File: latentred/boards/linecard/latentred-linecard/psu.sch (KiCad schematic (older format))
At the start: 56 parts, among them U1 MCP1703T-3302E, U2 LTC3374-QFN, U3 SI7050, U4 LTC2451, U5 INA226, U6 INA226, U7 INA226

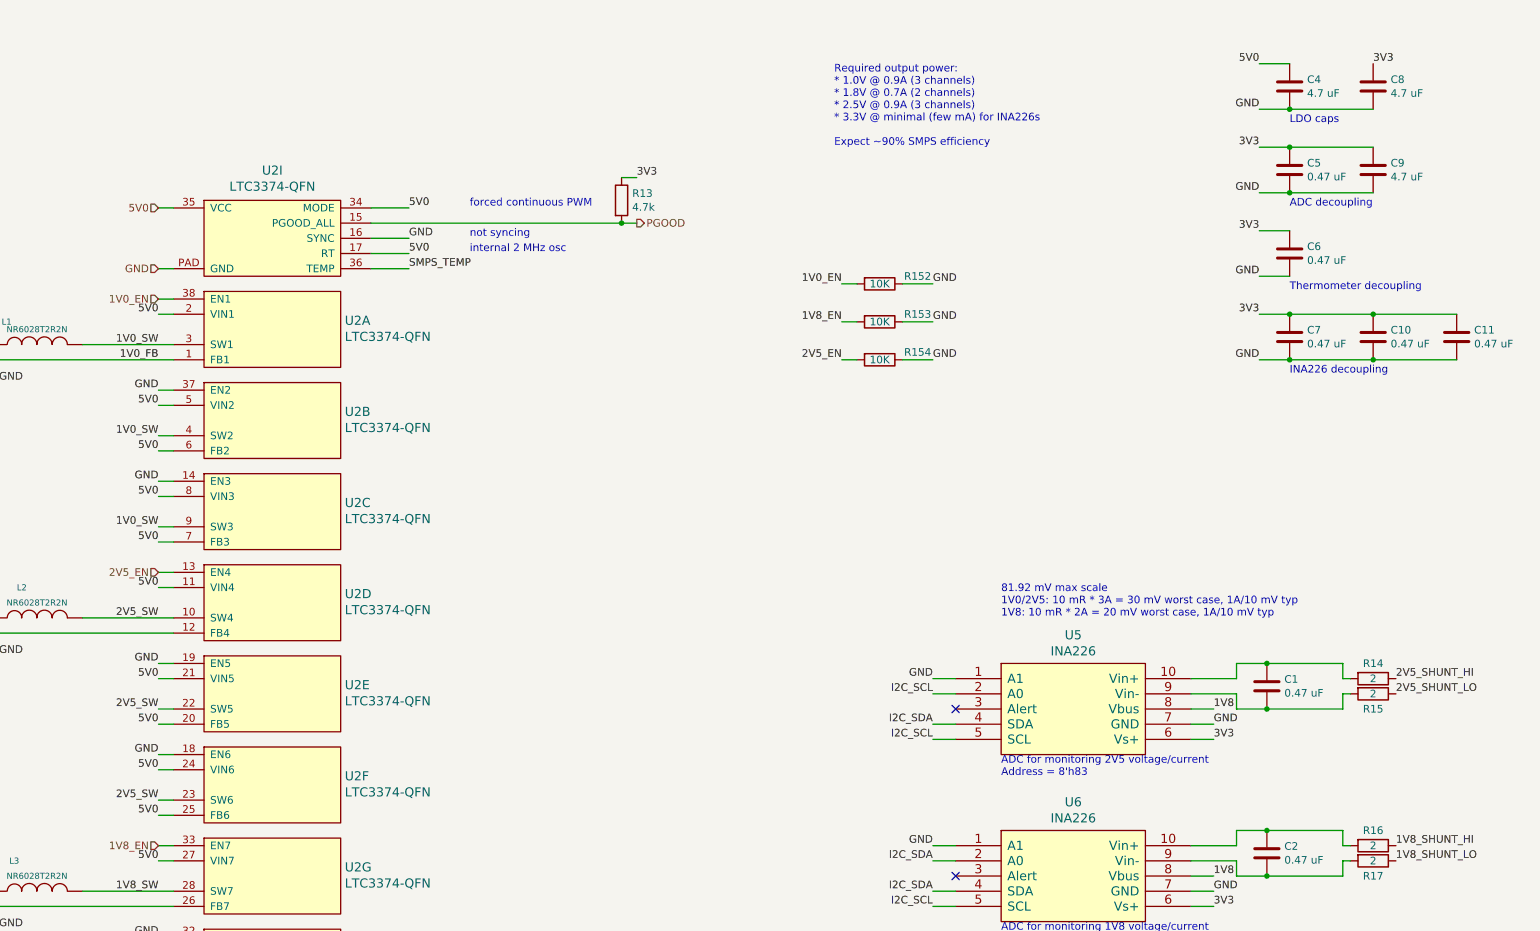
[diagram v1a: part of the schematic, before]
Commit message: Continued initial line card layout
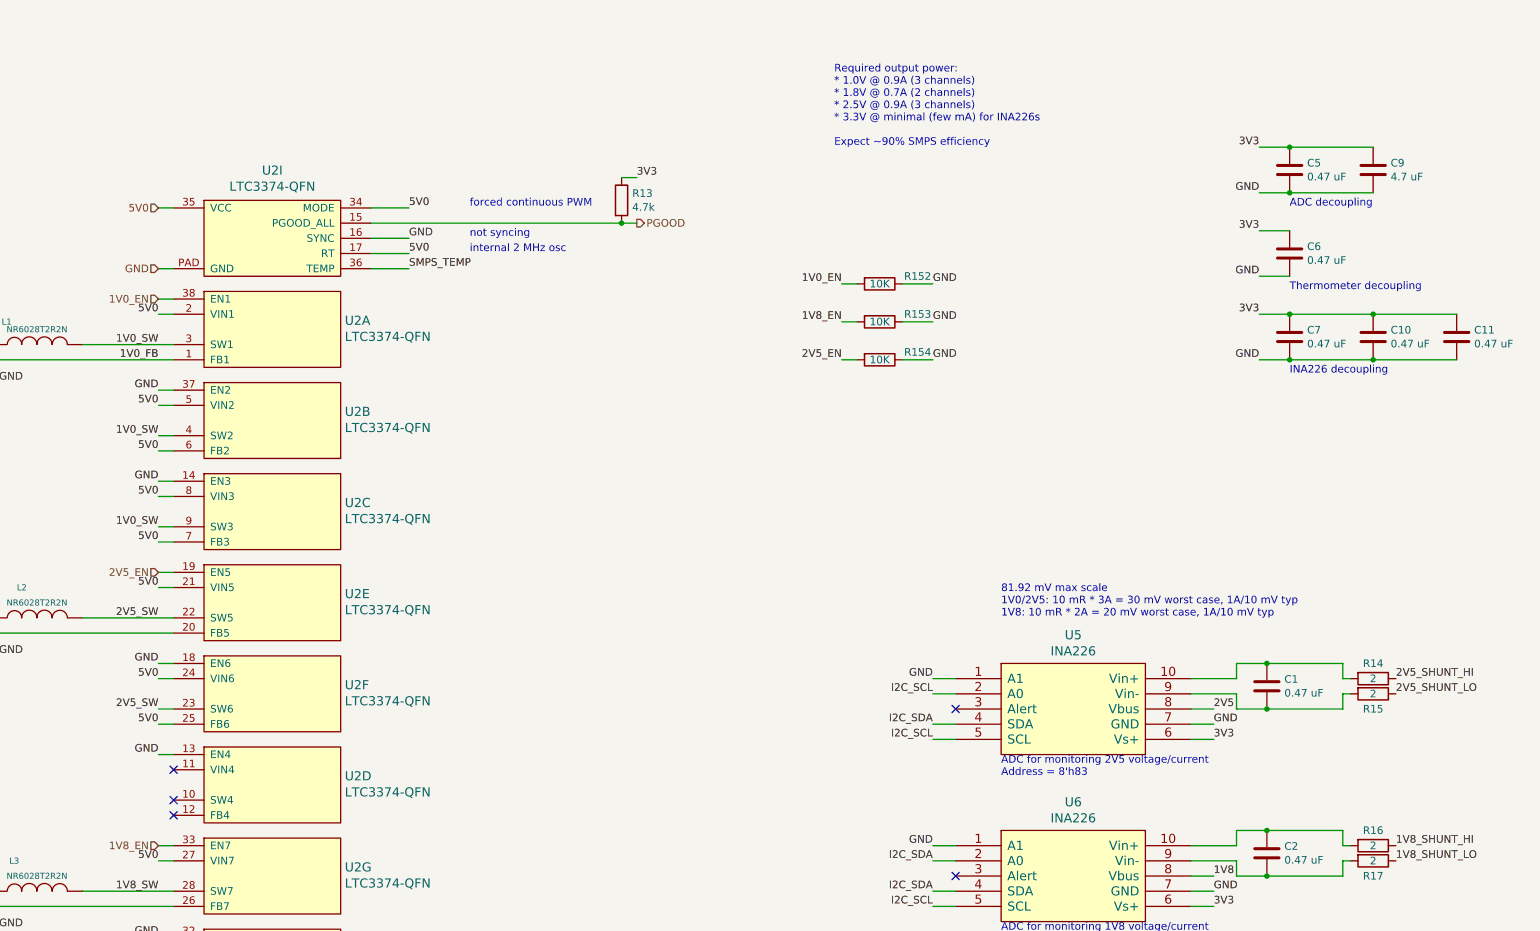
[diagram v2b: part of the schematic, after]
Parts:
- removed C4, C8: 4.7 uF, azonenberg_pcb:EIA_0603_CAP_NOSILK, symbol device:C
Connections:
- net 1V8: no longer U5.8 (Vbus)
- net 2V5: now also U5.8 (Vbus)
- net 2V5_EN: now also U2.19 (EN5); no longer U2.13 (EN4)
- net 2V5_SW: no longer U2.10 (SW4)
- net 5V0: no longer U2.11 (VIN4), U2.20 (FB5)
- net GND: now also U2.13 (EN4); no longer U2.19 (EN5)
- net at R11.2, R5.1: now also U2.20 (FB5); no longer U2.12 (FB4)
- no-connect marks 3 -> 6
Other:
- moved on the sheet: U2D, U2E, U2F
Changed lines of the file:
@@
 Sheet 2 3
 Title "LATENTRED 8-port 10/100/1000 Base-T Line Card"
-Date "2018-04-27"
+Date "2018-06-05"
 Rev "0.1"
 Comp "Andrew D. Zonenberg"
@@
 L power-azonenberg:LTC3374-QFN U2
 U 4 1 5AD42D7F
+P 6850 5850
+F 0 "U2" H 7777 6158 60  0000 L CNN
+F 1 "LTC3374-QFN" H 7777 6052 60  0000 L CNN
+F 2 "azonenberg_pcb:QFN_38_0.5MM_5x7MM" H 6850 5850 60  0001 C CNN
+F 3 "" H 6850 5850 60  0000 C CNN
+	4    6850 5850
+	1    0    0    -1
+$EndComp
+$Comp
+L power-azonenberg:LTC3374-QFN U2
+U 5 1 5AD42DF1
 P 6850 4650
 F 0 "U2" H 7777 4958 60  0000 L CNN
@@
 F 2 "azonenberg_pcb:QFN_38_0.5MM_5x7MM" H 6850 4650 60  0001 C CNN
 F 3 "" H 6850 4650 60  0000 C CNN
-	4    6850 4650
+	5    6850 4650
 	1    0    0    -1
 $EndComp
 $Comp
 L power-azonenberg:LTC3374-QFN U2
-U 5 1 5AD42DF1
+U 6 1 5AD42E61
 P 6850 5250
 F 0 "U2" H 7777 5558 60  0000 L CNN
@@
 F 2 "azonenberg_pcb:QFN_38_0.5MM_5x7MM" H 6850 5250 60  0001 C CNN
 F 3 "" H 6850 5250 60  0000 C CNN
-	5    6850 5250
-	1    0    0    -1
-$EndComp
-$Comp
-L power-azonenberg:LTC3374-QFN U2
-U 6 1 5AD42E61
-P 6850 5850
-F 0 "U2" H 7777 6158 60  0000 L CNN
-F 1 "LTC3374-QFN" H 7777 6052 60  0000 L CNN
-F 2 "azonenberg_pcb:QFN_38_0.5MM_5x7MM" H 6850 5850 60  0001 C CNN
-F 3 "" H 6850 5850 60  0000 C CNN
-	6    6850 5850
+	6    6850 5250
 	1    0    0    -1
 $EndComp
@@
 Wire Wire Line
 	6550 4900 6650 4900
-Text Label 6550 5500 2    50   ~ 0
-5V0
-Wire Wire Line
-	6550 5500 6650 5500
 Text Label 6550 6100 2    50   ~ 0
 5V0
@@
 Wire Wire Line
 	2450 10400 2000 10400
-$Comp
-L device:C C4
-U 1 1 5AD4D5DE
-P 14000 1000
-F 0 "C4" H 14115 1046 50  0000 L CNN
-F 1 "4.7 uF" H 14115 955 50  0000 L CNN
-F 2 "azonenberg_pcb:EIA_0603_CAP_NOSILK" H 14038 850 50  0001 C CNN
-F 3 "" H 14000 1000 50  0001 C CNN
-	1    14000 1000
-	1    0    0    -1
-$EndComp
-Text Notes 14000 1250 0    50   ~ 0
-LDO caps
-Text Label 13800 850  2    50   ~ 0
-5V0
-Text Label 13800 1150 2    50   ~ 0
-GND
-Wire Wire Line
-	13800 1150 14000 1150
-Wire Wire Line
-	13800 850  14000 850
-Text Label 14550 850  0    50   ~ 0
-3V3
-$Comp
-L device:C C8
-U 1 1 5AD4ECA1
-P 14550 1000
-F 0 "C8" H 14665 1046 50  0000 L CNN
-F 1 "4.7 uF" H 14665 955 50  0000 L CNN
-F 2 "azonenberg_pcb:EIA_0603_CAP_NOSILK" H 14588 850 50  0001 C CNN
-F 3 "" H 14550 1000 50  0001 C CNN
-	1    14550 1000
-	1    0    0    -1
-$EndComp
-Wire Wire Line
-	14000 1150 14550 1150
-Connection ~ 14000 1150
 Text Notes 14000 1800 0    50   ~ 0
 ADC decoupling
@@
 2V5_SHUNT_HI
 Text Label 13500 5100 0    50   ~ 0
-1V8
+2V5
 Wire Wire Line
 	13350 5100 13500 5100
@@
 Wire Wire Line
 	6550 5200 6650 5200
-Text Label 6550 5800 2    50   ~ 0
-5V0
-Wire Wire Line
-	6550 5800 6650 5800
 Text Label 6550 7000 2    50   ~ 0
 5V0
@@
 Wire Wire Line
 	6550 5100 6650 5100
-Text Label 6550 5700 2    50   ~ 0
-2V5_SW
-Wire Wire Line
-	6550 5700 6650 5700
 Text Label 6550 3900 2    50   ~ 0
 1V0_SW
@@
 Wire Wire Line
 	11650 2800 11450 2800
+NoConn ~ 6650 5500
+NoConn ~ 6650 5700
+NoConn ~ 6650 5800
 $EndSCHEMATC

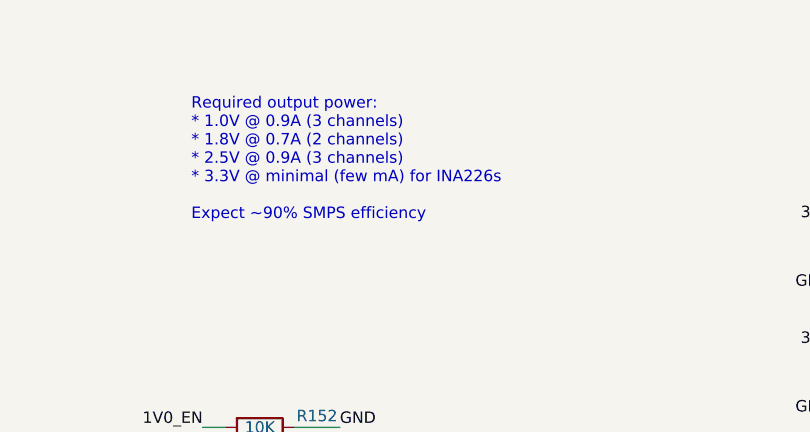
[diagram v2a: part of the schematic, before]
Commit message: Line card: updates to text descriptions at top level
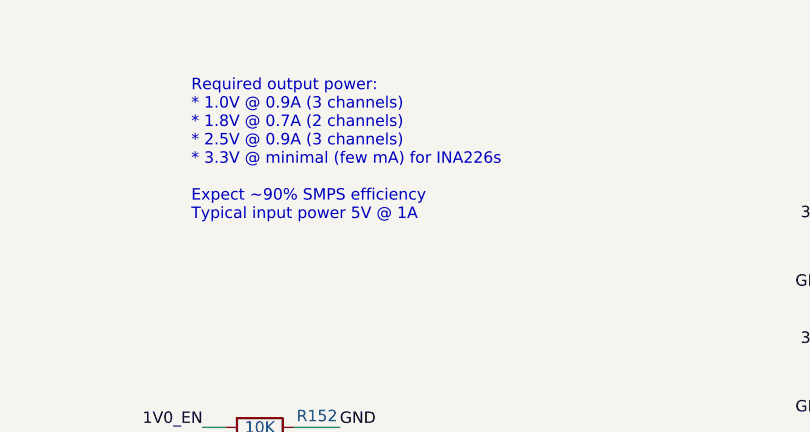
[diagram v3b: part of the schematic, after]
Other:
- note added: "Required output power: \n* 1.0V @ 0.9A (3 channels)\n* 1.8V @ 0.7A (2 channels)\n* 2.5V @ 0.9A (3 channels)\n* 3.3V @ minimal (few mA) for INA226s\n\nExpect ~~90% SMPS efficiency\nTypical input power 5V @ 1A"
- note removed: "Required output power: \n* 1.0V @ 0.9A (3 channels)\n* 1.8V @ 0.7A (2 channels)\n* 2.5V @ 0.9A (3 channels)\n* 3.3V @ minimal (few mA) for INA226s\n\nExpect ~~90% SMPS efficiency"
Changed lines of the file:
@@
 EESchema Schematic File Version 4
 LIBS:latentred-linecard-cache
-EELAYER 26 0
+EELAYER 30 0
 EELAYER END
 $Descr A3 16535 11693
@@
 $EndComp
 Text Notes 11000 1400 0    50   ~ 0
-Required output power: \n* 1.0V @ 0.9A (3 channels)\n* 1.8V @ 0.7A (2 channels)\n* 2.5V @ 0.9A (3 channels)\n* 3.3V @ minimal (few mA) for INA226s\n\nExpect ~~90% SMPS efficiency
+Required output power: \n* 1.0V @ 0.9A (3 channels)\n* 1.8V @ 0.7A (2 channels)\n* 2.5V @ 0.9A (3 channels)\n* 3.3V @ minimal (few mA) for INA226s\n\nExpect ~~90% SMPS efficiency\nTypical input power 5V @ 1A
 Text HLabel 6550 1800 0    50   Input ~ 0
 5V0
